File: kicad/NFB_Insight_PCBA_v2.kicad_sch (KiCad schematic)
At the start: 0 parts

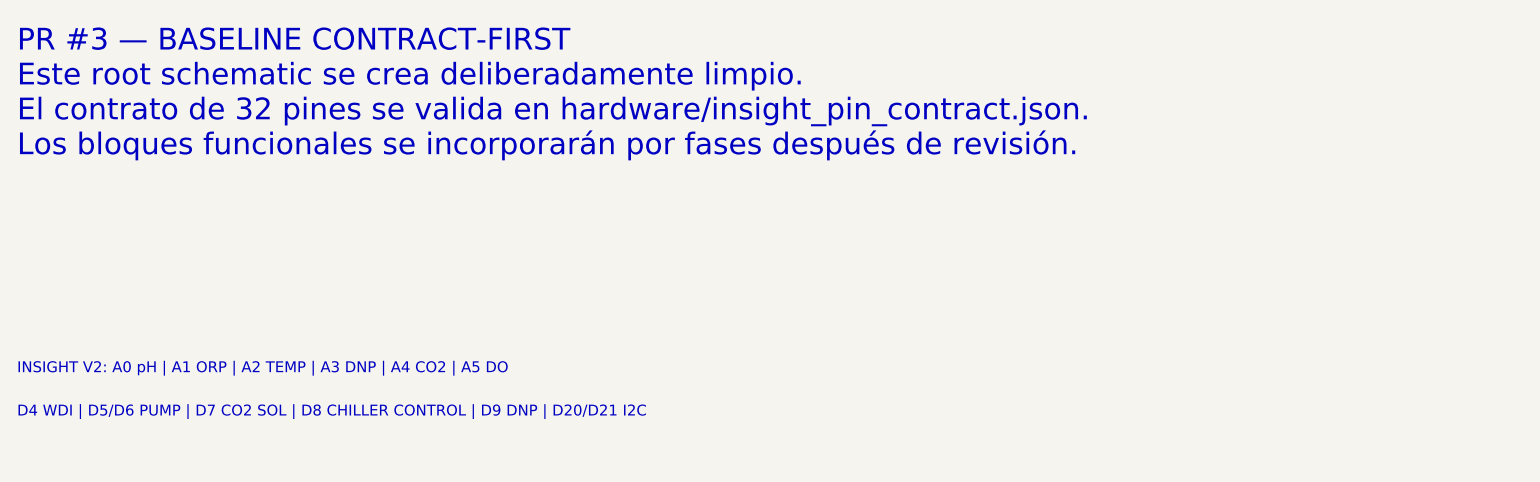
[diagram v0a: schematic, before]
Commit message: sensores: corregir interfaces reales de Insight (#5)
Corrige el baseline eléctrico de sensores contra documentación oficial: señales acondicionadas para pH/ORP/DO, A2/D16 como DS18B20 1-Wire, escalamiento seguro de entradas analógicas y MPX5700AP bloqueado para reemplazo antes de fabricación.
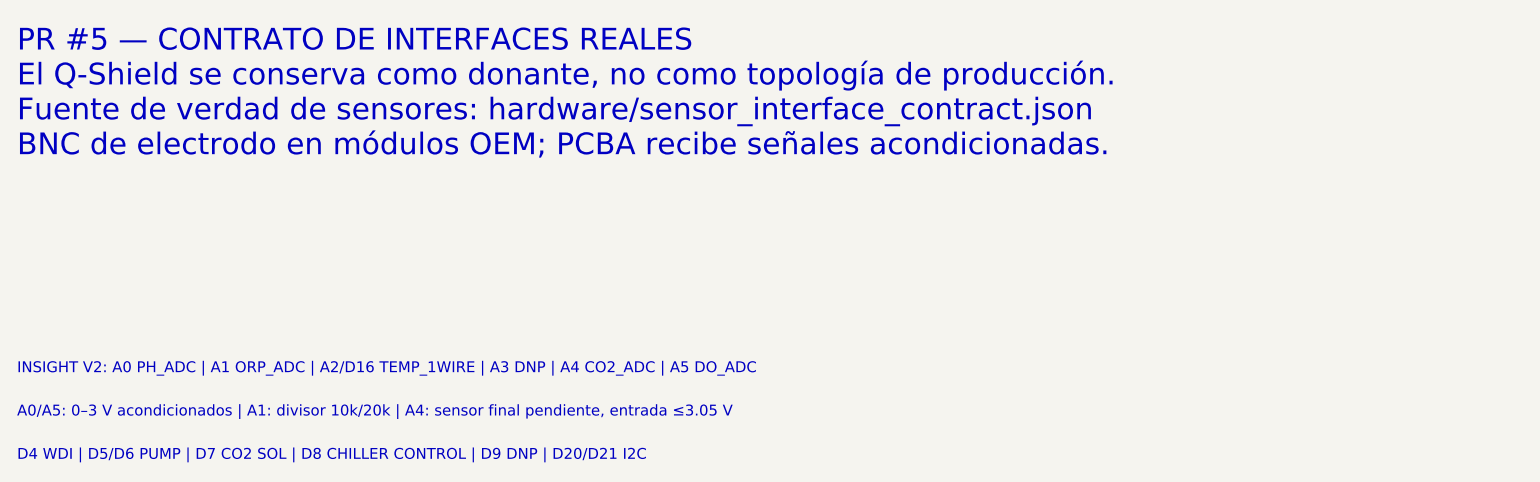
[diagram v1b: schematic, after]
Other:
- note added: "A0/A5: 0–3 V acondicionados | A1: divisor 10k/20k | A4: sensor final pendiente, entrada ≤3.05 V"
- note added: "INSIGHT V2: A0 PH_ADC | A1 ORP_ADC | A2/D16 TEMP_1WIRE | A3 DNP | A4 CO2_ADC | A5 DO_ADC"
- note added: "PR #5 — CONTRATO DE INTERFACES REALES El Q-Shield se conserva como donante, no como topología de producción. Fuente de verdad de sensores: hardware/sensor_interface_contract.json BNC de electrodo en módulos OEM; PCBA recibe señales acondicionadas."
- note removed: "INSIGHT V2: A0 pH | A1 ORP | A2 TEMP | A3 DNP | A4 CO2 | A5 DO"
- note removed: "PR #3 — BASELINE CONTRACT-FIRST Este root schematic se crea deliberadamente limpio. El contrato de 32 pines se valida en hardware/insight_pin_contract.json. Los bloques funcionales se incorporarán por fases después de revisión."
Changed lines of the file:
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@@
   (version 20250114)
   (generator "nfb_contract_bootstrap")
-  (generator_version "1.0")
+  (generator_version "1.1")
   (paper "A3")
   (title_block
     (title "NFB Insight PCBA v2 — Contrato Eléctrico Base")
     (date "2026-08-11")
-    (rev "0.3")
+    (rev "0.5")
     (company "Cafelium SRL / Nebula Ecosystem")
-    (comment 1 "Baseline contract-first para Arduino UNO Q")
-    (comment 2 "Pinout fuente de verdad: hardware/insight_pin_contract.json")
-    (comment 3 "A3 y D9 reservados/DNP en Insight")
-    (comment 4 "Sin migración de bloques funcionales en PR #3")
+    (comment 1 "Contrato corregido PR #5: interfaces reales de sensores")
+    (comment 2 "Pinout: hardware/insight_pin_contract.json")
+    (comment 3 "Sensores: hardware/sensor_interface_contract.json")
+    (comment 4 "A2/D16 = TEMP_1WIRE; A3 y D9 reservados/DNP")
   )
-  (text "PR #3 — BASELINE CONTRACT-FIRST\nEste root schematic se crea deliberadamente limpio.\nEl contrato de 32 pines se valida en hardware/insight_pin_contract.json.\nLos bloques funcionales se incorporarán por fases después de revisión."
-    (exclude_from_sim no)
+  (text "PR #5 — CONTRATO DE INTERFACES REALES\nEl Q-Shield se conserva como donante, no como topología de producción.\nFuente de verdad de sensores: hardware/sensor_interface_contract.json\nBNC de electrodo en módulos OEM; PCBA recibe señales acondicionadas."
     (at 50.8 50.8 0)
     (effects
@@
     )
   )
-  (text "INSIGHT V2: A0 pH | A1 ORP | A2 TEMP | A3 DNP | A4 CO2 | A5 DO"
-    (exclude_from_sim no)
+  (text "INSIGHT V2: A0 PH_ADC | A1 ORP_ADC | A2/D16 TEMP_1WIRE | A3 DNP | A4 CO2_ADC | A5 DO_ADC"
     (at 50.8 76.2 0)
     (effects
@@
     )
   )
-  (text "D4 WDI | D5/D6 PUMP | D7 CO2 SOL | D8 CHILLER CONTROL | D9 DNP | D20/D21 I2C"
-    (exclude_from_sim no)
+  (text "A0/A5: 0–3 V acondicionados | A1: divisor 10k/20k | A4: sensor final pendiente, entrada ≤3.05 V"
     (at 50.8 81.28 0)
     (effects
       (font (size 1.27 1.27))
+      (justify left bottom)
+    )
+  )
+  (text "D4 WDI | D5/D6 PUMP | D7 CO2 SOL | D8 CHILLER CONTROL | D9 DNP | D20/D21 I2C"
+    (at 50.8 86.36 0)
+    (effects
+      (font (size 1.27 1.27))

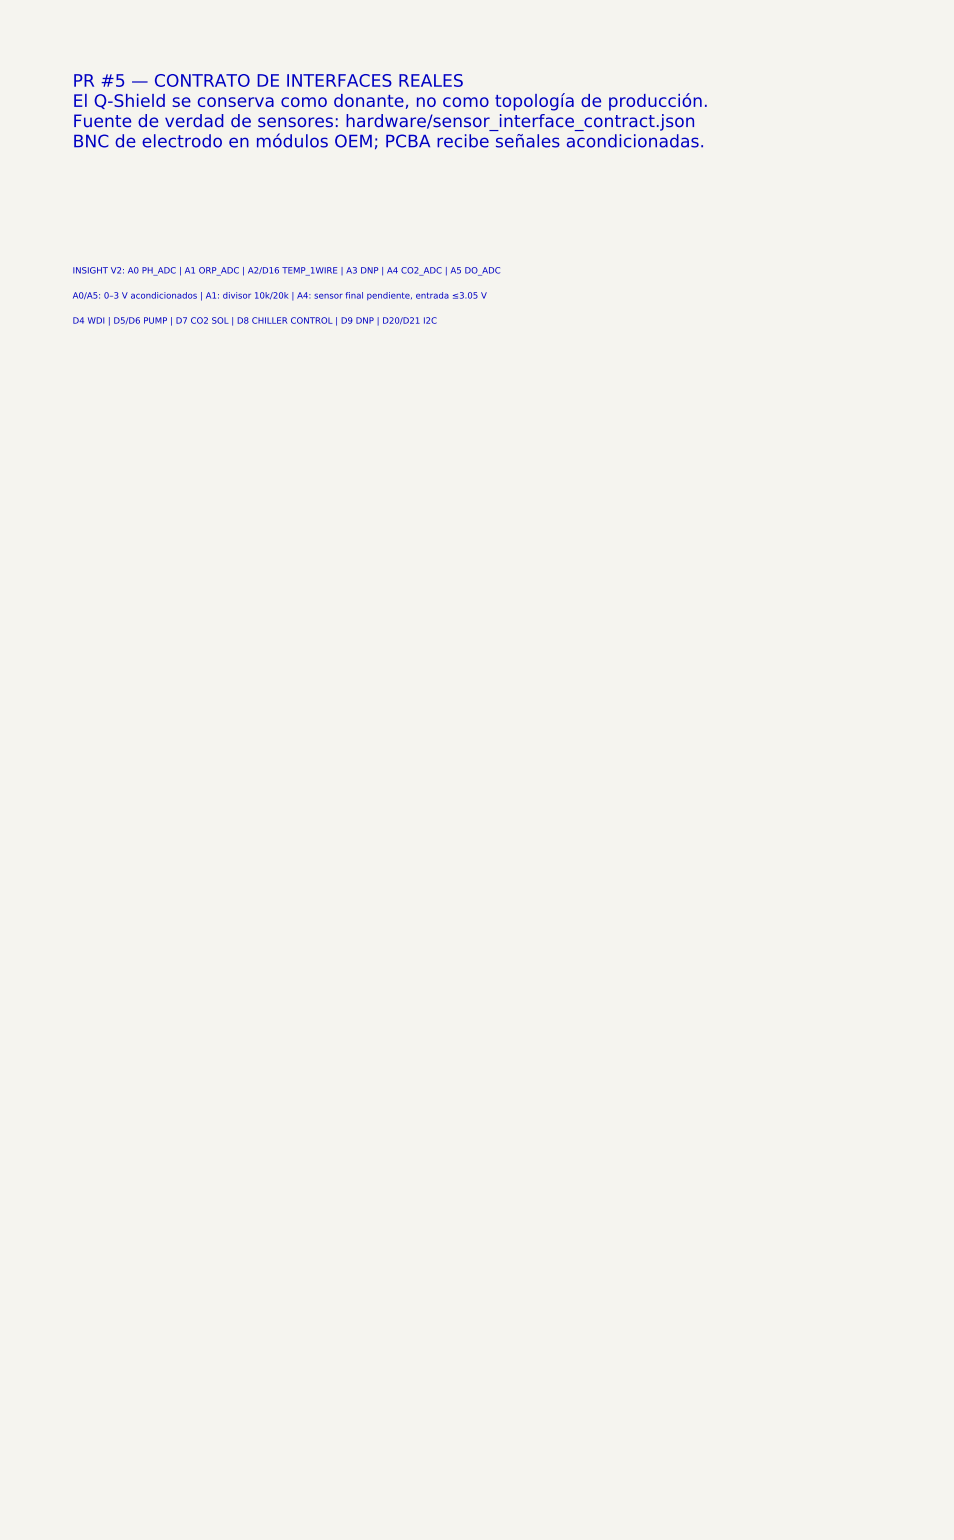
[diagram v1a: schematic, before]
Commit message: sensores: congelar netlist de producción Z1 (#6)
Congela Z1 para NFB Insight V2: Honeywell MPRLS0030PA00002A por I2C 0x28, A4 DNP, interfaces pH/ORP/TEMP/DO, conectores JST XH, ESD, filtros, BOM/netlist machine-readable y gates de validación. Placement, routing, potencia y cambios de firmware permanecen fuera de alcance.
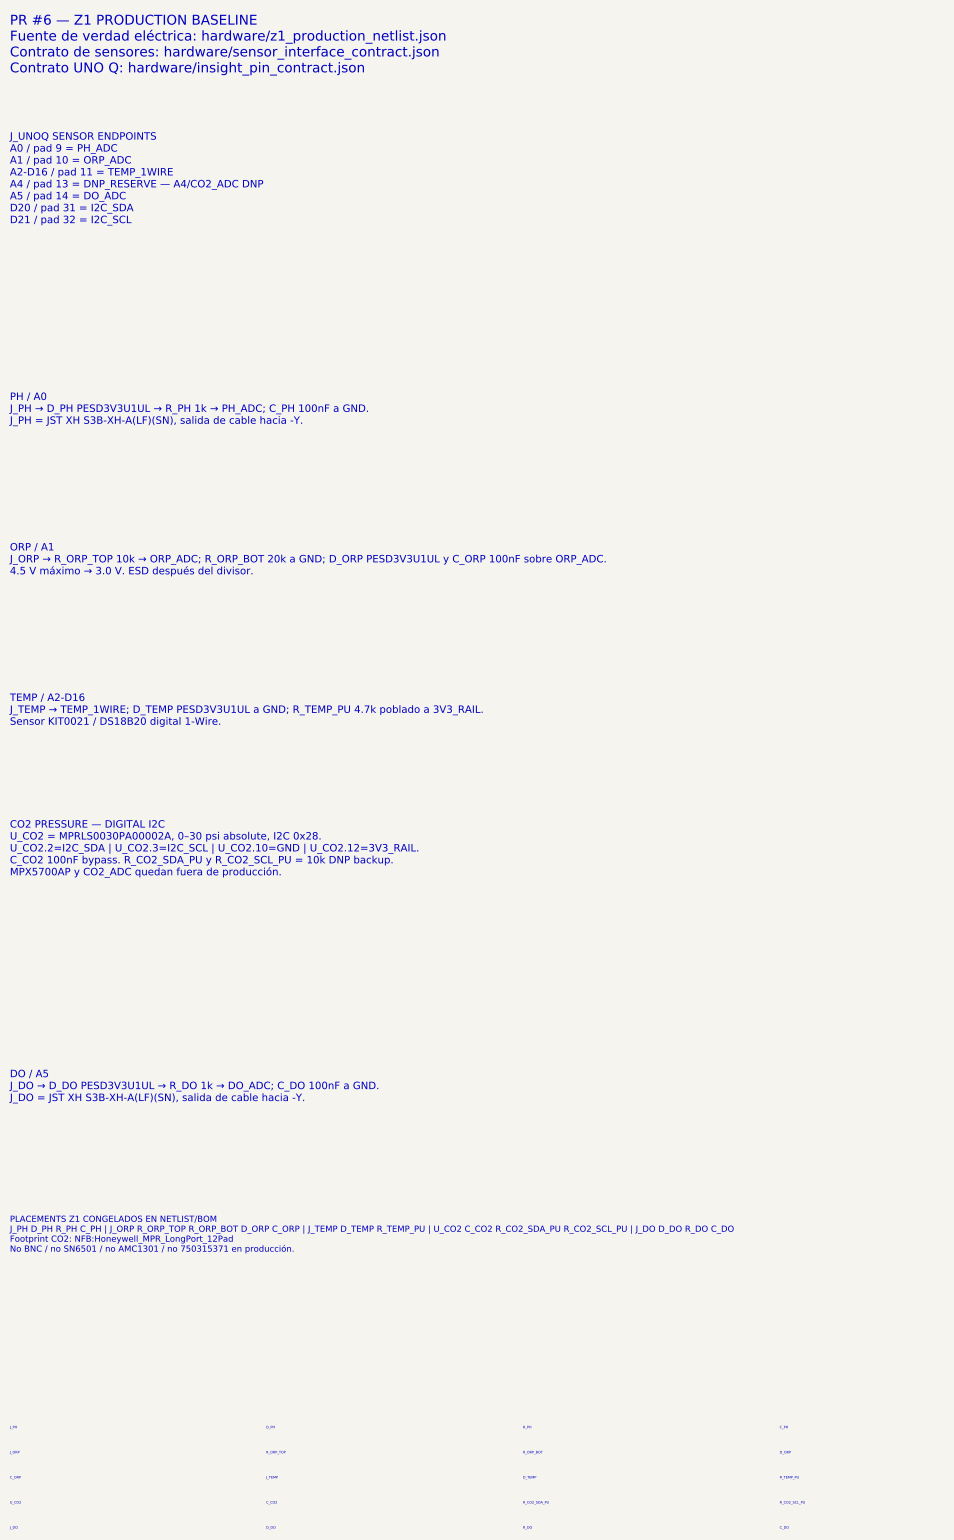
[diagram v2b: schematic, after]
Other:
- note added: "CO2 PRESSURE — DIGITAL I2C U_CO2 = MPRLS0030PA00002A, 0–30 psi absolute, I2C 0x28. U_CO2.2=I2C_SDA | U_CO2.3=I2C_SCL | U_CO2.10=GND | U_CO2.12=3V3_RAIL. C_CO2 100nF bypass. R_CO2_SDA_PU y R_CO2_SCL_PU = 10k DNP backup. MPX5700AP y CO2_ADC quedan fuera de producción."
- note added: "C_CO2"
- note added: "C_DO"
- note added: "C_ORP"
- note added: "C_PH"
- note added: "DO / A5 J_DO → D_DO PESD3V3U1UL → R_DO 1k → DO_ADC; C_DO 100nF a GND. J_DO = JST XH S3B-XH-A(LF)(SN), salida de cable hacia -Y."
- note added: "D_DO"
- note added: "D_ORP"
- note added: "D_PH"
- note added: "D_TEMP"
- note added: "J_DO"
- note added: "J_ORP"
- note added: "J_PH"
- note added: "J_TEMP"
- note added: "J_UNOQ SENSOR ENDPOINTS A0 / pad 9 = PH_ADC A1 / pad 10 = ORP_ADC A2-D16 / pad 11 = TEMP_1WIRE A4 / pad 13 = DNP_RESERVE — A4/CO2_ADC DNP A5 / pad 14 = DO_ADC D20 / pad 31 = I2C_SDA D21 / pad 32 = I2C_SCL"
- note added: "ORP / A1 J_ORP → R_ORP_TOP 10k → ORP_ADC; R_ORP_BOT 20k a GND; D_ORP PESD3V3U1UL y C_ORP 100nF sobre ORP_ADC. 4.5 V máximo → 3.0 V. ESD después del divisor."
- note added: "PH / A0 J_PH → D_PH PESD3V3U1UL → R_PH 1k → PH_ADC; C_PH 100nF a GND. J_PH = JST XH S3B-XH-A(LF)(SN), salida de cable hacia -Y."
- note added: "PLACEMENTS Z1 CONGELADOS EN NETLIST/BOM J_PH D_PH R_PH C_PH | J_ORP R_ORP_TOP R_ORP_BOT D_ORP C_ORP | J_TEMP D_TEMP R_TEMP_PU | U_CO2 C_CO2 R_CO2_SDA_PU R_CO2_SCL_PU | J_DO D_DO R_DO C_DO Footprint CO2: NFB:Honeywell_MPR_LongPort_12Pad No BNC / no SN6501 / no AMC1301 / no 750315371 en producción."
- note added: "PR #6 — Z1 PRODUCTION BASELINE Fuente de verdad eléctrica: hardware/z1_production_netlist.json Contrato de sensores: hardware/sensor_interface_contract.json Contrato UNO Q: hardware/insight_pin_contract.json"
- note added: "R_CO2_SCL_PU"
- note added: "R_CO2_SDA_PU"
- note added: "R_DO"
- note added: "R_ORP_BOT"
- note added: "R_ORP_TOP"
- note added: "R_PH"
- note added: "R_TEMP_PU"
- note added: "TEMP / A2-D16 J_TEMP → TEMP_1WIRE; D_TEMP PESD3V3U1UL a GND; R_TEMP_PU 4.7k poblado a 3V3_RAIL. Sensor KIT0021 / DS18B20 digital 1-Wire."
- note added: "U_CO2"
- note removed: "A0/A5: 0–3 V acondicionados | A1: divisor 10k/20k | A4: sensor final pendiente, entrada ≤3.05 V"
- note removed: "D4 WDI | D5/D6 PUMP | D7 CO2 SOL | D8 CHILLER CONTROL | D9 DNP | D20/D21 I2C"
- note removed: "INSIGHT V2: A0 PH_ADC | A1 ORP_ADC | A2/D16 TEMP_1WIRE | A3 DNP | A4 CO2_ADC | A5 DO_ADC"
- note removed: "PR #5 — CONTRATO DE INTERFACES REALES El Q-Shield se conserva como donante, no como topología de producción. Fuente de verdad de sensores: hardware/sensor_interface_contract.json BNC de electrodo en módulos OEM; PCBA recibe señales acondicionadas."
- title: NFB Insight PCBA v2 — Contrato Eléctrico Base -> NFB Insight PCBA v2 — Z1 Sensor Production Contract
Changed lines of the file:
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@@
 (kicad_sch
   (version 20250114)
-  (generator "nfb_contract_bootstrap")
-  (generator_version "1.1")
+  (generator "nfb_pr6_contract")
+  (generator_version "1.4")
   (paper "A3")
   (title_block
-    (title "NFB Insight PCBA v2 — Contrato Eléctrico Base")
+    (title "NFB Insight PCBA v2 — Z1 Sensor Production Contract")
     (date "2026-08-11")
-    (rev "0.5")
+    (rev "0.6.5")
     (company "Cafelium SRL / Nebula Ecosystem")
-    (comment 1 "Contrato corregido PR #5: interfaces reales de sensores")
-    (comment 2 "Pinout: hardware/insight_pin_contract.json")
-    (comment 3 "Sensores: hardware/sensor_interface_contract.json")
-    (comment 4 "A2/D16 = TEMP_1WIRE; A3 y D9 reservados/DNP")
+    (comment 1 "PR #6 — contrato discreto Z1 gobernado por hardware/z1_production_netlist.json")
+    (comment 2 "BOM: bom/insight_z1_production_bom.csv")
+    (comment 3 "A4/CO2_ADC DNP; CO2=MPRLS0030PA00002A I2C 0x28")
+    (comment 4 "Hoja raíz contractual; placement/routing fuera de alcance")
   )
-  (text "PR #5 — CONTRATO DE INTERFACES REALES\nEl Q-Shield se conserva como donante, no como topología de producción.\nFuente de verdad de sensores: hardware/sensor_interface_contract.json\nBNC de electrodo en módulos OEM; PCBA recibe señales acondicionadas."
-    (at 50.8 50.8 0)
-    (effects
-      (font (size 2.54 2.54))
-      (justify left bottom)
-    )
+  (text "PR #6 — Z1 PRODUCTION BASELINE\nFuente de verdad eléctrica: hardware/z1_production_netlist.json\nContrato de sensores: hardware/sensor_interface_contract.json\nContrato UNO Q: hardware/insight_pin_contract.json"
+    (exclude_from_sim no)
+    (at 38.1 35.56 0)
+    (effects (font (size 2.0 2.0)) (justify left bottom))
   )
-  (text "INSIGHT V2: A0 PH_ADC | A1 ORP_ADC | A2/D16 TEMP_1WIRE | A3 DNP | A4 CO2_ADC | A5 DO_ADC"
-    (at 50.8 76.2 0)
-    (effects
-      (font (size 1.27 1.27))
-      (justify left bottom)
-    )
+  (text "J_UNOQ SENSOR ENDPOINTS\nA0 / pad 9 = PH_ADC\nA1 / pad 10 = ORP_ADC\nA2-D16 / pad 11 = TEMP_1WIRE\nA4 / pad 13 = DNP_RESERVE — A4/CO2_ADC DNP\nA5 / pad 14 = DO_ADC\nD20 / pad 31 = I2C_SDA\nD21 / pad 32 = I2C_SCL"
+    (exclude_from_sim no)
+    (at 38.1 66.04 0)
+    (effects (font (size 1.5 1.5)) (justify left bottom))
   )
-  (text "A0/A5: 0–3 V acondicionados | A1: divisor 10k/20k | A4: sensor final pendiente, entrada ≤3.05 V"
-    (at 50.8 81.28 0)
-    (effects
-      (font (size 1.27 1.27))
-      (justify left bottom)
-    )
+  (text "PH / A0\nJ_PH → D_PH PESD3V3U1UL → R_PH 1k → PH_ADC; C_PH 100nF a GND.\nJ_PH = JST XH S3B-XH-A(LF)(SN), salida de cable hacia -Y."
+    (exclude_from_sim no)
+    (at 38.1 106.68 0)
+    (effects (font (size 1.5 1.5)) (justify left bottom))
   )
-  (text "D4 WDI | D5/D6 PUMP | D7 CO2 SOL | D8 CHILLER CONTROL | D9 DNP | D20/D21 I2C"
-    (at 50.8 86.36 0)
-    (effects
-      (font (size 1.27 1.27))
-      (justify left bottom)
-    )
+  (text "ORP / A1\nJ_ORP → R_ORP_TOP 10k → ORP_ADC; R_ORP_BOT 20k a GND; D_ORP PESD3V3U1UL y C_ORP 100nF sobre ORP_ADC.\n4.5 V máximo → 3.0 V. ESD después del divisor."
+    (exclude_from_sim no)
+    (at 38.1 137.16 0)
+    (effects (font (size 1.5 1.5)) (justify left bottom))
   )
+  (text "TEMP / A2-D16\nJ_TEMP → TEMP_1WIRE; D_TEMP PESD3V3U1UL a GND; R_TEMP_PU 4.7k poblado a 3V3_RAIL.\nSensor KIT0021 / DS18B20 digital 1-Wire."
+    (exclude_from_sim no)
+    (at 38.1 167.64 0)
+    (effects (font (size 1.5 1.5)) (justify left bottom))
+  )
+  (text "CO2 PRESSURE — DIGITAL I2C\nU_CO2 = MPRLS0030PA00002A, 0–30 psi absolute, I2C 0x28.\nU_CO2.2=I2C_SDA | U_CO2.3=I2C_SCL | U_CO2.10=GND | U_CO2.12=3V3_RAIL.\nC_CO2 100nF bypass. R_CO2_SDA_PU y R_CO2_SCL_PU = 10k DNP backup.\nMPX5700AP y CO2_ADC quedan fuera de producción."
+    (exclude_from_sim no)
+    (at 38.1 198.12 0)
+    (effects (font (size 1.5 1.5)) (justify left bottom))
+  )
+  (text "DO / A5\nJ_DO → D_DO PESD3V3U1UL → R_DO 1k → DO_ADC; C_DO 100nF a GND.\nJ_DO = JST XH S3B-XH-A(LF)(SN), salida de cable hacia -Y."
+    (exclude_from_sim no)
+    (at 38.1 243.84 0)
+    (effects (font (size 1.5 1.5)) (justify left bottom))
+  )
+  (text "PLACEMENTS Z1 CONGELADOS EN NETLIST/BOM\nJ_PH D_PH R_PH C_PH | J_ORP R_ORP_TOP R_ORP_BOT D_ORP C_ORP | J_TEMP D_TEMP R_TEMP_PU | U_CO2 C_CO2 R_CO2_SDA_PU R_CO2_SCL_PU | J_DO D_DO R_DO C_DO\nFootprint CO2: NFB:Honeywell_MPR_LongPort_12Pad\nNo BNC / no SN6501 / no AMC1301 / no 750315371 en producción."
+    (exclude_from_sim no)
+    (at 38.1 274.32 0)
+    (effects (font (size 1.25 1.25)) (justify left bottom))
+  )
+  (text "J_PH" (exclude_from_sim no) (at 38.1 310 0) (effects (font (size 0.5 0.5)) (justify left bottom)))
+  (text "D_PH" (exclude_from_sim no) (at 90 310 0) (effects (font (size 0.5 0.5)) (justify left bottom)))
+  (text "R_PH" (exclude_from_sim no) (at 142 310 0) (effects (font (size 0.5 0.5)) (justify left bottom)))
+  (text "C_PH" (exclude_from_sim no) (at 194 310 0) (effects (font (size 0.5 0.5)) (justify left bottom)))
+  (text "J_ORP" (exclude_from_sim no) (at 38.1 315.08 0) (effects (font (size 0.5 0.5)) (justify left bottom)))
+  (text "R_ORP_TOP" (exclude_from_sim no) (at 90 315.08 0) (effects (font (size 0.5 0.5)) (justify left bottom)))
+  (text "R_ORP_BOT" (exclude_from_sim no) (at 142 315.08 0) (effects (font (size 0.5 0.5)) (justify left bottom)))
+  (text "D_ORP" (exclude_from_sim no) (at 194 315.08 0) (effects (font (size 0.5 0.5)) (justify left bottom)))
+  (text "C_ORP" (exclude_from_sim no) (at 38.1 320.16 0) (effects (font (size 0.5 0.5)) (justify left bottom)))
+  (text "J_TEMP" (exclude_from_sim no) (at 90 320.16 0) (effects (font (size 0.5 0.5)) (justify left bottom)))
+  (text "D_TEMP" (exclude_from_sim no) (at 142 320.16 0) (effects (font (size 0.5 0.5)) (justify left bottom)))
+  (text "R_TEMP_PU" (exclude_from_sim no) (at 194 320.16 0) (effects (font (size 0.5 0.5)) (justify left bottom)))
+  (text "U_CO2" (exclude_from_sim no) (at 38.1 325.24 0) (effects (font (size 0.5 0.5)) (justify left bottom)))
+  (text "C_CO2" (exclude_from_sim no) (at 90 325.24 0) (effects (font (size 0.5 0.5)) (justify left bottom)))
+  (text "R_CO2_SDA_PU" (exclude_from_sim no) (at 142 325.24 0) (effects (font (size 0.5 0.5)) (justify left bottom)))
+  (text "R_CO2_SCL_PU" (exclude_from_sim no) (at 194 325.24 0) (effects (font (size 0.5 0.5)) (justify left bottom)))
+  (text "J_DO" (exclude_from_sim no) (at 38.1 330.32 0) (effects (font (size 0.5 0.5)) (justify left bottom)))
+  (text "D_DO" (exclude_from_sim no) (at 90 330.32 0) (effects (font (size 0.5 0.5)) (justify left bottom)))
+  (text "R_DO" (exclude_from_sim no) (at 142 330.32 0) (effects (font (size 0.5 0.5)) (justify left bottom)))
+  (text "C_DO" (exclude_from_sim no) (at 194 330.32 0) (effects (font (size 0.5 0.5)) (justify left bottom)))
   (sheet_instances
-    (path "/"
-      (page "1")
-    )
+    (path "/" (page "1"))
   )
 )
